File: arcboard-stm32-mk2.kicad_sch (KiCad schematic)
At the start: 88 parts, among them J1 Conn_01x04_Socket, J17 Conn_01x04_Socket, J2 Conn_01x04_Socket, J3 Conn_01x04_Socket, J5 Conn_01x02_Socket, J6 Conn_01x02_Socket, J7 Conn_01x02_Socket, U1 XC6210B332MR-G, U13 2N7002, U14 W25Q128JVSIQTR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

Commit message: re-organized the bottom section to fit a piezo
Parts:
- added J4: Conn_01x02_Socket, Connector_JST:JST_PH_S2B-PH-K_1x02_P2.00mm_Horizontal, symbol Connector:Conn_01x02_Socket
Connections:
- net +3V3: no longer U15.1 (A)
- net VO+: now also J4.2 (Pin_2)
- net VO-: now also J4.1 (Pin_1)
- net at D11.2 (A), J5.2 (Pin_2), R15.1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: no longer U15.3 (C)
- no-connect marks 32 -> 34
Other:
- note added: "Uhhhh why no pin4"
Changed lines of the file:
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@@
 		)
 	)
+	(text "Uhhhh why no pin4"
+		(exclude_from_sim no)
+		(at 323.088 369.062 0)
+		(effects
+			(font
+				(size 1.27 1.27)
+			)
+		)
+	)
 	(text "LCD power"
 		(exclude_from_sim no)
@@
 	)
 	(junction
+		(at 279.4 384.81)
+		(diameter 0)
+		(color 0 0 0 0)
+	)
+	(junction
 		(at 275.59 175.26)
 		(diameter 0)
@@
 	)
 	(junction
-		(at 464.82 107.95)
-		(diameter 0)
-		(color 0 0 0 0)
-	)
-	(junction
 		(at 86.36 374.65)
 		(diameter 0)
@@
 	)
 	(junction
+		(at 281.94 387.35)
+		(diameter 0)
+		(color 0 0 0 0)
+	)
+	(junction
 		(at 168.91 242.57)
 		(diameter 0)
@@
 	)
 	(junction
-		(at 482.6 107.95)
-		(diameter 0)
-		(color 0 0 0 0)
-	)
-	(junction
 		(at 81.28 374.65)
 		(diameter 0)
@@
 	)
 	(no_connect
+		(at 469.9 120.65)
+	)
+	(no_connect
 		(at 392.43 163.83)
 	)
@@
 	)
 	(no_connect
+		(at 477.52 120.65)
+	)
+	(no_connect
 		(at 328.93 232.41)
 	)
@@
 	(wire
 		(pts
-			(xy 477.52 118.11) (xy 482.6 118.11)
-		)
-		(stroke
-			(width 0)
-			(type default)
-		)
-	)
-	(wire
-		(pts
 			(xy 168.91 207.01) (xy 172.72 207.01)
 		)
@@
 	(wire
 		(pts
-			(xy 464.82 118.11) (xy 469.9 118.11)
-		)
-		(stroke
-			(width 0)
-			(type default)
-		)
-	)
-	(wire
-		(pts
 			(xy 170.18 250.19) (xy 172.72 250.19)
 		)
@@
 	(wire
 		(pts
-			(xy 278.13 387.35) (xy 283.21 387.35)
+			(xy 278.13 387.35) (xy 281.94 387.35)
 		)
 		(stroke
@@
 	(wire
 		(pts
+			(xy 276.86 396.24) (xy 281.94 396.24)
+		)
+		(stroke
+			(width 0)
+			(type default)
+		)
+	)
+	(wire
+		(pts
 			(xy 389.89 280.67) (xy 392.43 280.67)
 		)
@@
 	(wire
 		(pts
-			(xy 278.13 384.81) (xy 283.21 384.81)
+			(xy 278.13 384.81) (xy 279.4 384.81)
 		)
 		(stroke
@@
 	(wire
 		(pts
-			(xy 482.6 107.95) (xy 482.6 118.11)
-		)
-		(stroke
-			(width 0)
-			(type default)
-		)
-	)
-	(wire
-		(pts
 			(xy 284.48 175.26) (xy 294.64 175.26)
 		)
@@
 	(wire
 		(pts
+			(xy 281.94 387.35) (xy 283.21 387.35)
+		)
+		(stroke
+			(width 0)
+			(type default)
+		)
+	)
+	(wire
+		(pts
 			(xy 549.91 162.56) (xy 549.91 166.37)
 		)
@@
 	(wire
 		(pts
+			(xy 276.86 393.7) (xy 279.4 393.7)
+		)
+		(stroke
+			(width 0)
+			(type default)
+		)
+	)
+	(wire
+		(pts
 			(xy 374.65 148.59) (xy 374.65 151.13)
 		)
@@
 	(wire
 		(pts
+			(xy 281.94 387.35) (xy 281.94 396.24)
+		)
+		(stroke
+			(width 0)
+			(type default)
+		)
+	)
+	(wire
+		(pts
 			(xy 161.29 234.95) (xy 161.29 242.57)
 		)
@@
 	(wire
 		(pts
+			(xy 469.9 118.11) (xy 469.9 120.65)
+		)
+		(stroke
+			(width 0)
+			(type default)
+		)
+	)
+	(wire
+		(pts
 			(xy 168.91 245.11) (xy 172.72 245.11)
 		)
@@
 	(wire
 		(pts
+			(xy 279.4 384.81) (xy 283.21 384.81)
+		)
+		(stroke
+			(width 0)
+			(type default)
+		)
+	)
+	(wire
+		(pts
 			(xy 334.01 247.65) (xy 339.09 247.65)
 		)
@@
 	(wire
 		(pts
+			(xy 279.4 384.81) (xy 279.4 393.7)
+		)
+		(stroke
+			(width 0)
+			(type default)
+		)
+	)
+	(wire
+		(pts
 			(xy 339.09 273.05) (xy 325.12 273.05)
 		)
@@
 	(wire
 		(pts
+			(xy 477.52 118.11) (xy 477.52 120.65)
+		)
+		(stroke
+			(width 0)
+			(type default)
+		)
+	)
+	(wire
+		(pts
 			(xy 389.89 163.83) (xy 392.43 163.83)
 		)
@@
 	(wire
 		(pts
-			(xy 464.82 107.95) (xy 464.82 118.11)
-		)
-		(stroke
-			(width 0)
-			(type default)
-		)
-	)
-	(wire
-		(pts
 			(xy 458.47 104.14) (xy 458.47 102.87)
 		)
@@
 					(unit 1)
 				)
+			)
+		)
+	)
+	(symbol
+		(lib_id "Connector:Conn_01x02_Socket")
+		(at 271.78 396.24 180)
+		(unit 1)
+		(exclude_from_sim no)
+		(in_bom yes)
+		(on_board yes)
+		(dnp no)
+		(fields_autoplaced yes)
+		(property "Reference" "J4"
+			(at 272.415 388.62 0)
+			(effects
+				(font
+					(size 1.27 1.27)
+				)
+			)
+		)
+		(property "Value" "Conn_01x02_Socket"
+			(at 272.415 391.16 0)
+			(effects
+				(font
+					(size 1.27 1.27)
+				)
+			)
+		)
+		(property "Footprint" "Connector_JST:JST_PH_S2B-PH-K_1x02_P2.00mm_Horizontal"
+			(at 271.78 396.24 0)
+			(effects
+				(font
+					(size 1.27 1.27)
+				)
+				(hide yes)
+			)
+		)
+		(property "Datasheet" "~"
+			(at 271.78 396.24 0)
+			(effects
+				(font
+					(size 1.27 1.27)
+				)
+				(hide yes)
+			)
+		)
+		(property "Description" "Generic connector, single row, 01x02, script generated"
+			(at 271.78 396.24 0)
+			(effects
+				(font
+					(size 1.27 1.27)
+				)
+				(hide yes)
+			)
+		)
+		(pin "2"
+		)
+		(pin "1"
+		)
+		(instances
+			(project ""
+				(path "/e3b5a64c-dc86-4c04-b1b0-762b30a6a8fe"
+					(reference "J4")
+					(unit 1)
+				)

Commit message: silkscreen work, adding lse crystal and vbat hookup
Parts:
- removed LOGO2: **REF, kicad-libraries:awesome-logo, symbol kicad-libraries:awesome-logo
- removed LOGO7: **REF, kicad-libraries:awesome-logo-25mm, symbol kicad-libraries:qmk-lite-logo
- added C29, C30: 12p, Capacitor_SMD:C_0402_1005Metric, symbol Device:C_Small
- added J8: Conn_01x02_Socket, Connector_JST:JST_PH_S2B-PH-K_1x02_P2.00mm_Horizontal, symbol Connector:Conn_01x02_Socket
- added U8: SC-32S32_768kHz20PPM7pF, kicad-libraries:OSC-SMD_L3.2-W1.5, symbol kicad-libraries:SC-32S32_768kHz20PPM7pF
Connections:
- net GND: now also C29.1, C30.1, J8.1 (Pin_1)
- net VBAT: now reaches U2.6 (VBAT)
- net VBAT: now also J8.2 (Pin_2)
- net LSE_OSC32_IN: now reaches U2.8 (PC14)
- net LSE_OSC32_IN: now also C30.2, U8.2
- net LSE_OSC32_OUT: now reaches U2.9 (PC15)
- net LSE_OSC32_OUT: now also C29.2, U8.1
- no-connect marks 34 -> 31
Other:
- note added: "Main USB in"
- note added: "Serial out"
- note removed: "Main USB"
- note removed: "Serial TRRS"

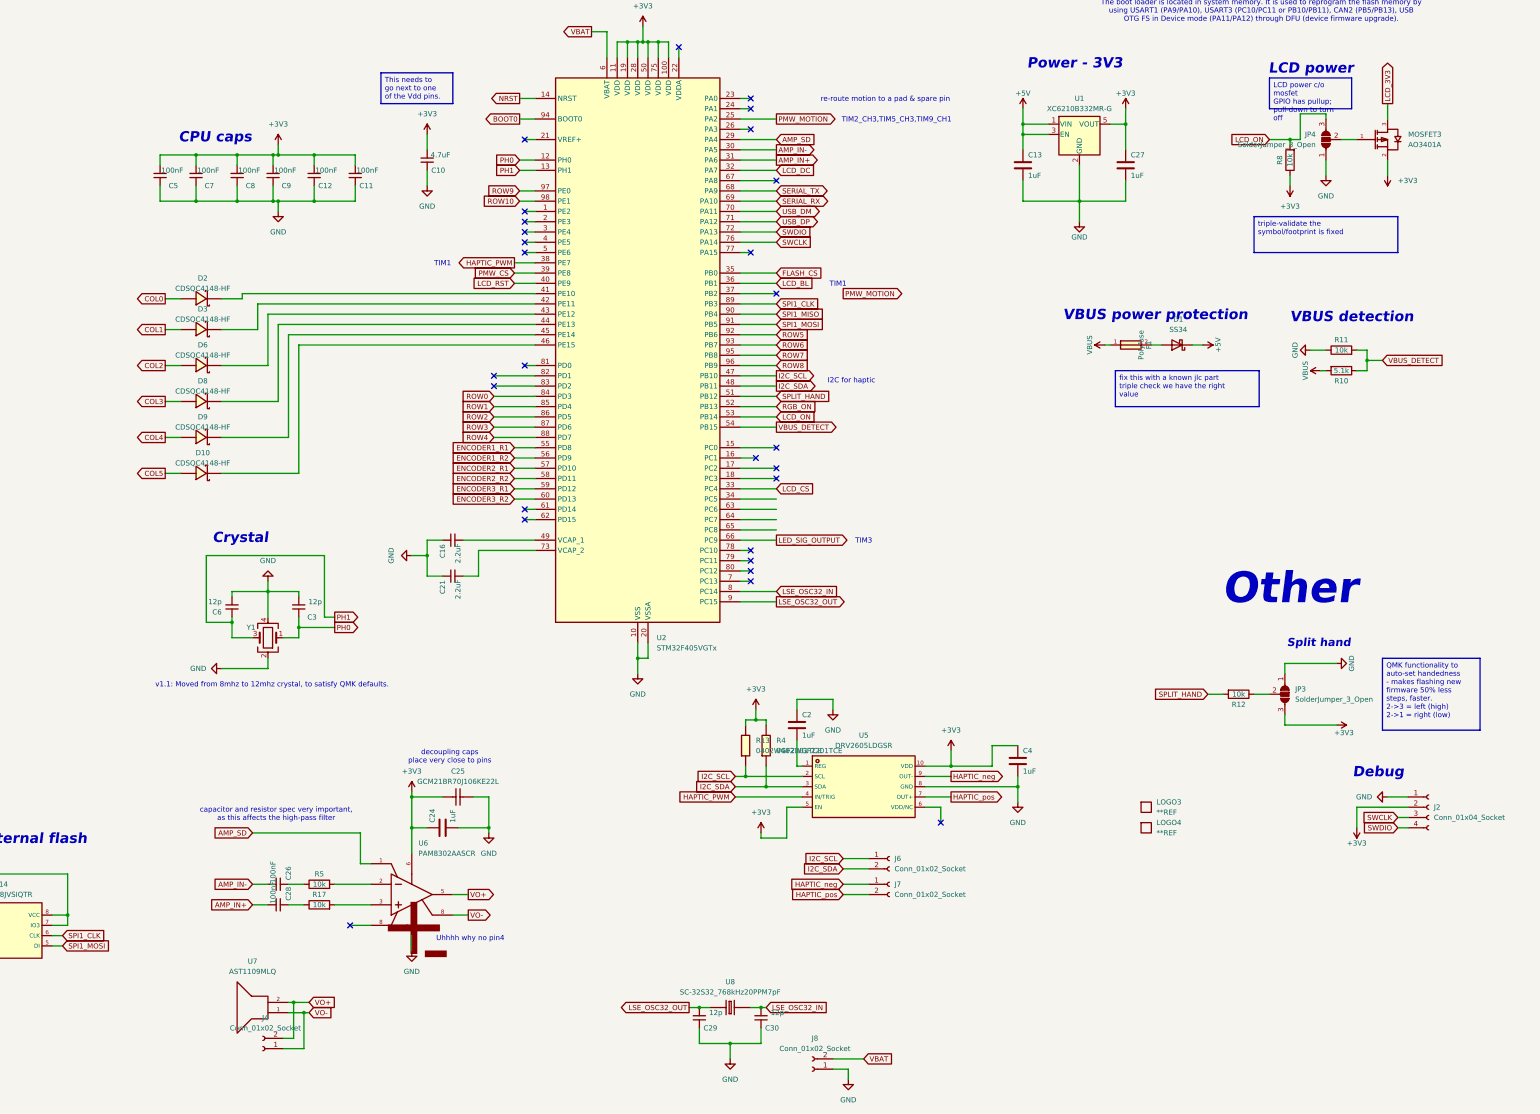
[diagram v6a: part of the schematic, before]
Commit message: fixing issues brought up by drashna, adding timer notation to schematic
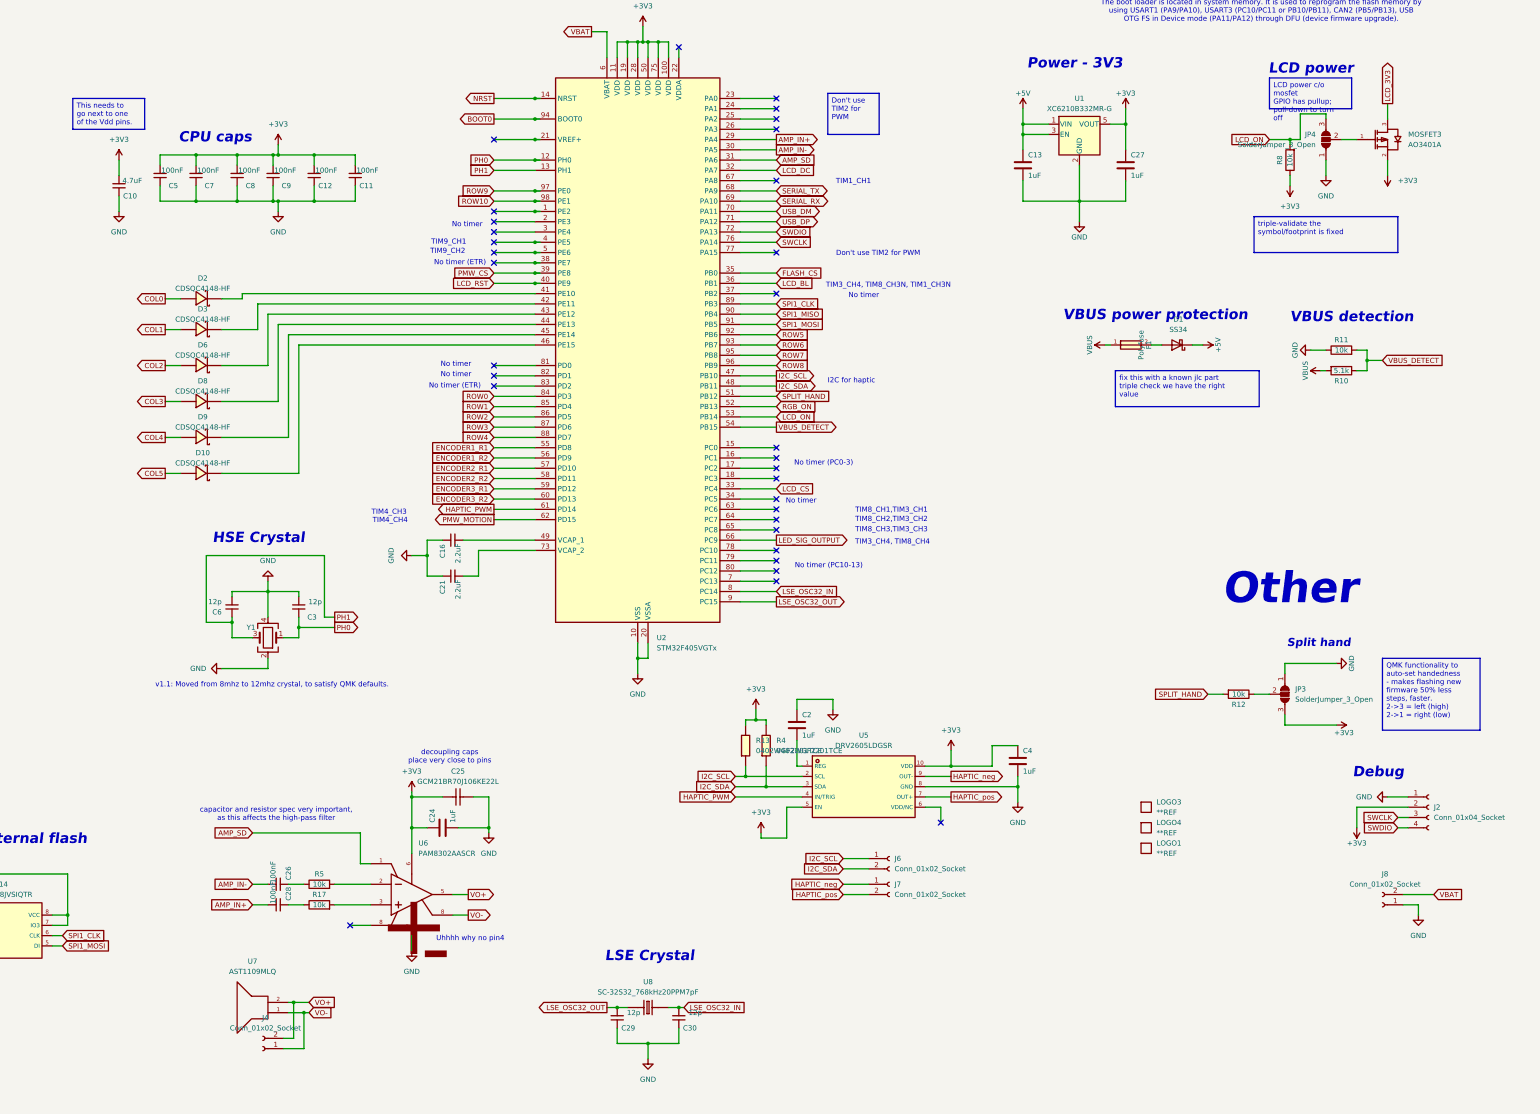
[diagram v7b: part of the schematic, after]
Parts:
- added LOGO1: **REF, kicad-libraries:awesome-logo, symbol kicad-libraries:awesome-logo
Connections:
- net AMP_IN+: now also U2.29 (PA4); no longer U2.31 (PA6)
- net AMP_SD: now also U2.31 (PA6); no longer U2.29 (PA4)
- net HAPTIC_PWM: now also U2.61 (PD14); no longer U2.38 (PE7)
- net PMW_MOTION: now also U2.62 (PD15); no longer U2.25 (PA2)
- no-connect marks 31 -> 35
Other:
- note added: "Don't use TIM2 for PWM"
- note added: "HSE Crystal"
- note added: "LSE Crystal"
- note added: "No timer"
- note added: "No timer (ETR)"
- note added: "No timer (PC0-3)"
- note added: "No timer (PC10-13)"
- note added: "TIM1_CH1"
- note added: "TIM3_CH4, TIM8_CH3N, TIM1_CH3N"
- note added: "TIM3_CH4, TIM8_CH4"
- note added: "TIM4_CH3"
- note added: "TIM4_CH4"
- note added: "TIM8_CH1,TIM3_CH1"
- note added: "TIM8_CH2,TIM3_CH2"
- note added: "TIM8_CH3,TIM3_CH3"
- note added: "TIM9_CH1"
- note added: "TIM9_CH2"
- note removed: "Crystal"
- note removed: "TIM1"
- note removed: "TIM2_CH3,TIM5_CH3,TIM9_CH1"
- note removed: "TIM3"
- note removed: "re-route motion to a pad & spare pin"
- moved on the sheet: C10, C29, C30, J8, U8

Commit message: fixing haptic driver missing another vdd, more
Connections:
- net +3V3: now also U5.6 (VDD/NC)
- no-connect marks 35 -> 34
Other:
- note added: "??? TIM3_CH4, TIM8_CH3N, TIM1_CH3N"
- note added: "Amplifier"
- note added: "DFU: RESET, BOOT"
- note added: "External VBAT"
- note added: "Haptic driver"
- note added: "MCU"
- note added: "Other outputs"
- note added: "Piezo"
- note removed: "DFU, RESET, BOOT"
- note removed: "MCU; power, timing, & boot"
- note removed: "Other"
- note removed: "TIM3_CH4, TIM8_CH3N, TIM1_CH3N"
- moved on the sheet: C1, C10, C11, C12, C13, C14, C15, C16, C18, C19, C2, C20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
